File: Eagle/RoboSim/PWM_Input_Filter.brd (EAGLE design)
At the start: 74.6 x 78.7 mm, 72 parts, among them IC1 TLV2772, IC2 TLV2772, IC3 TLV2772

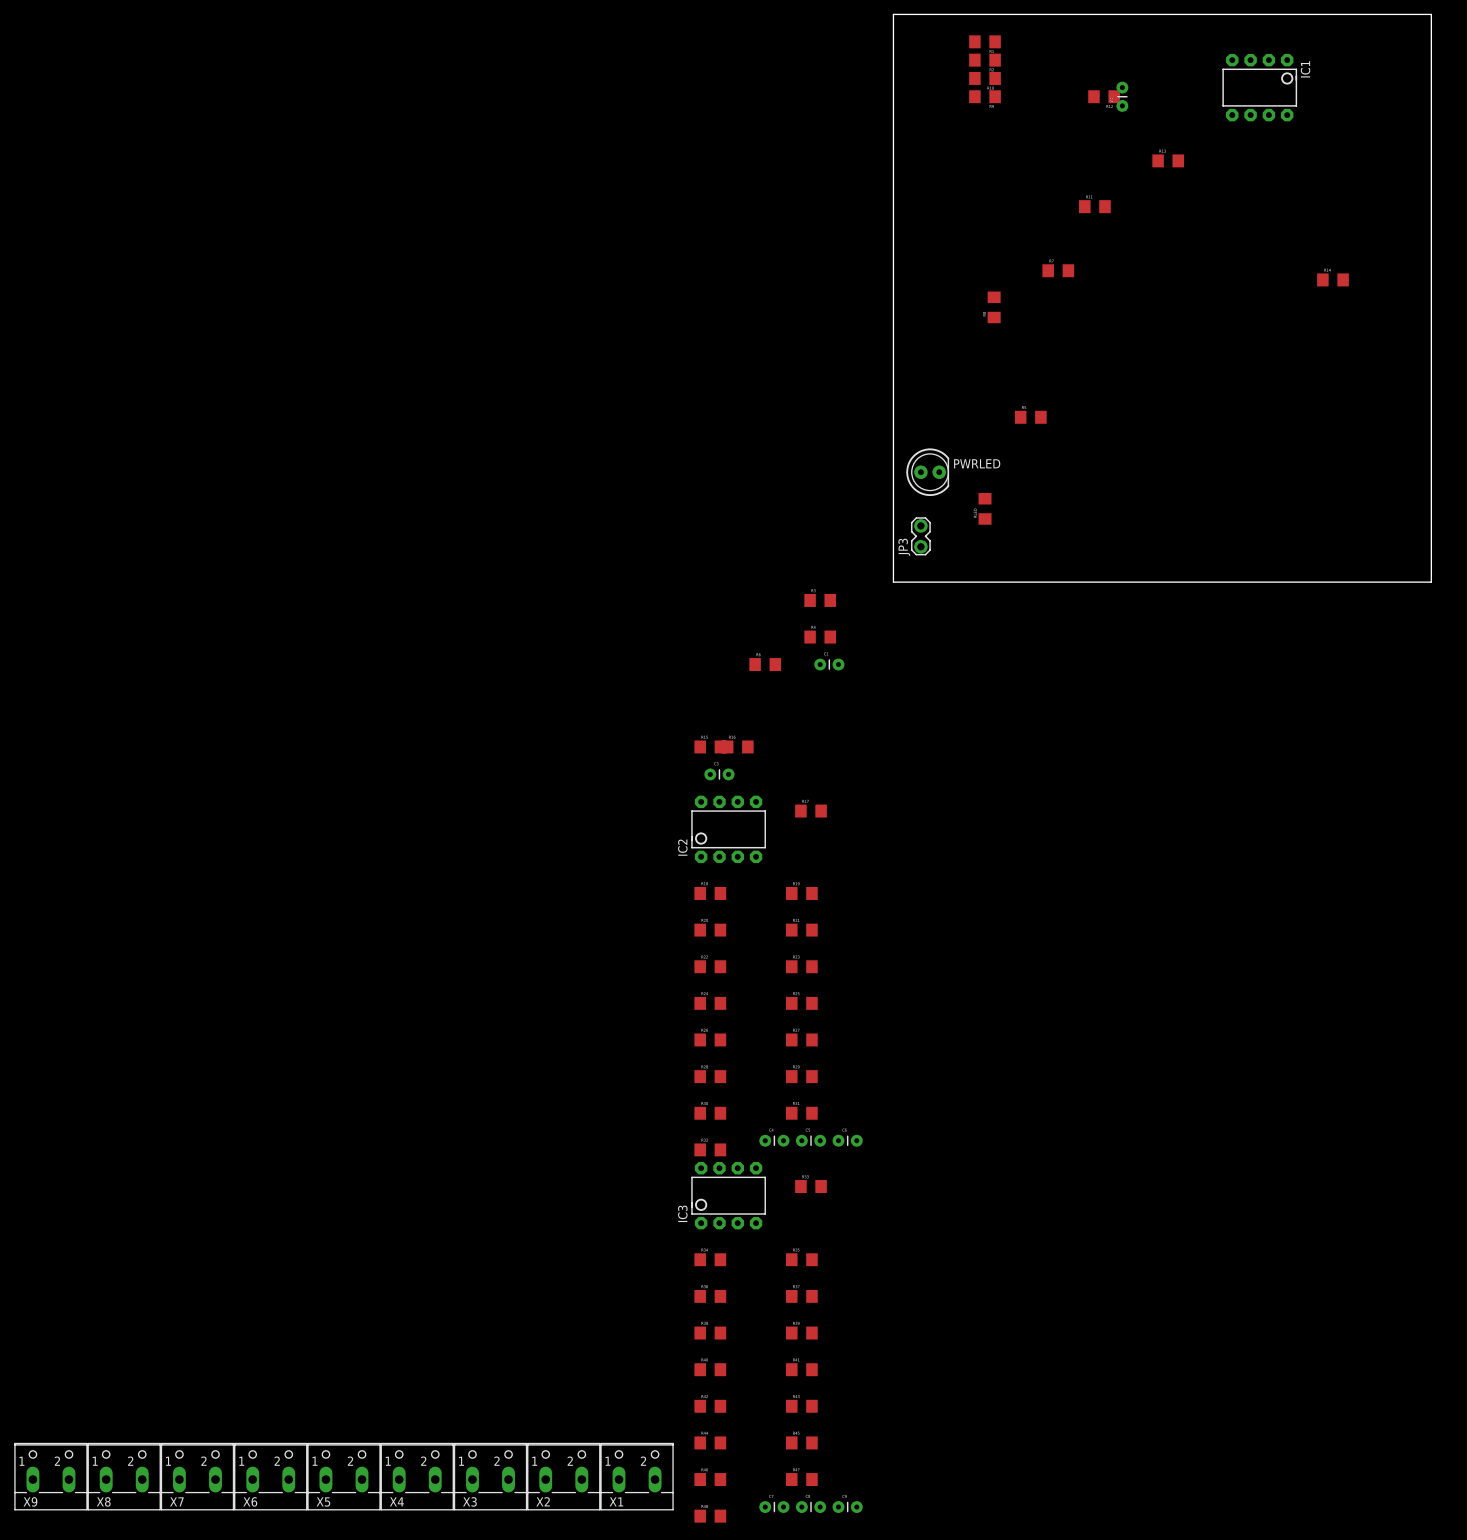
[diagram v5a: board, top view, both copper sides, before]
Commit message: trimmed pwm filter circuit schematic to just show two channels, fixed up schematic
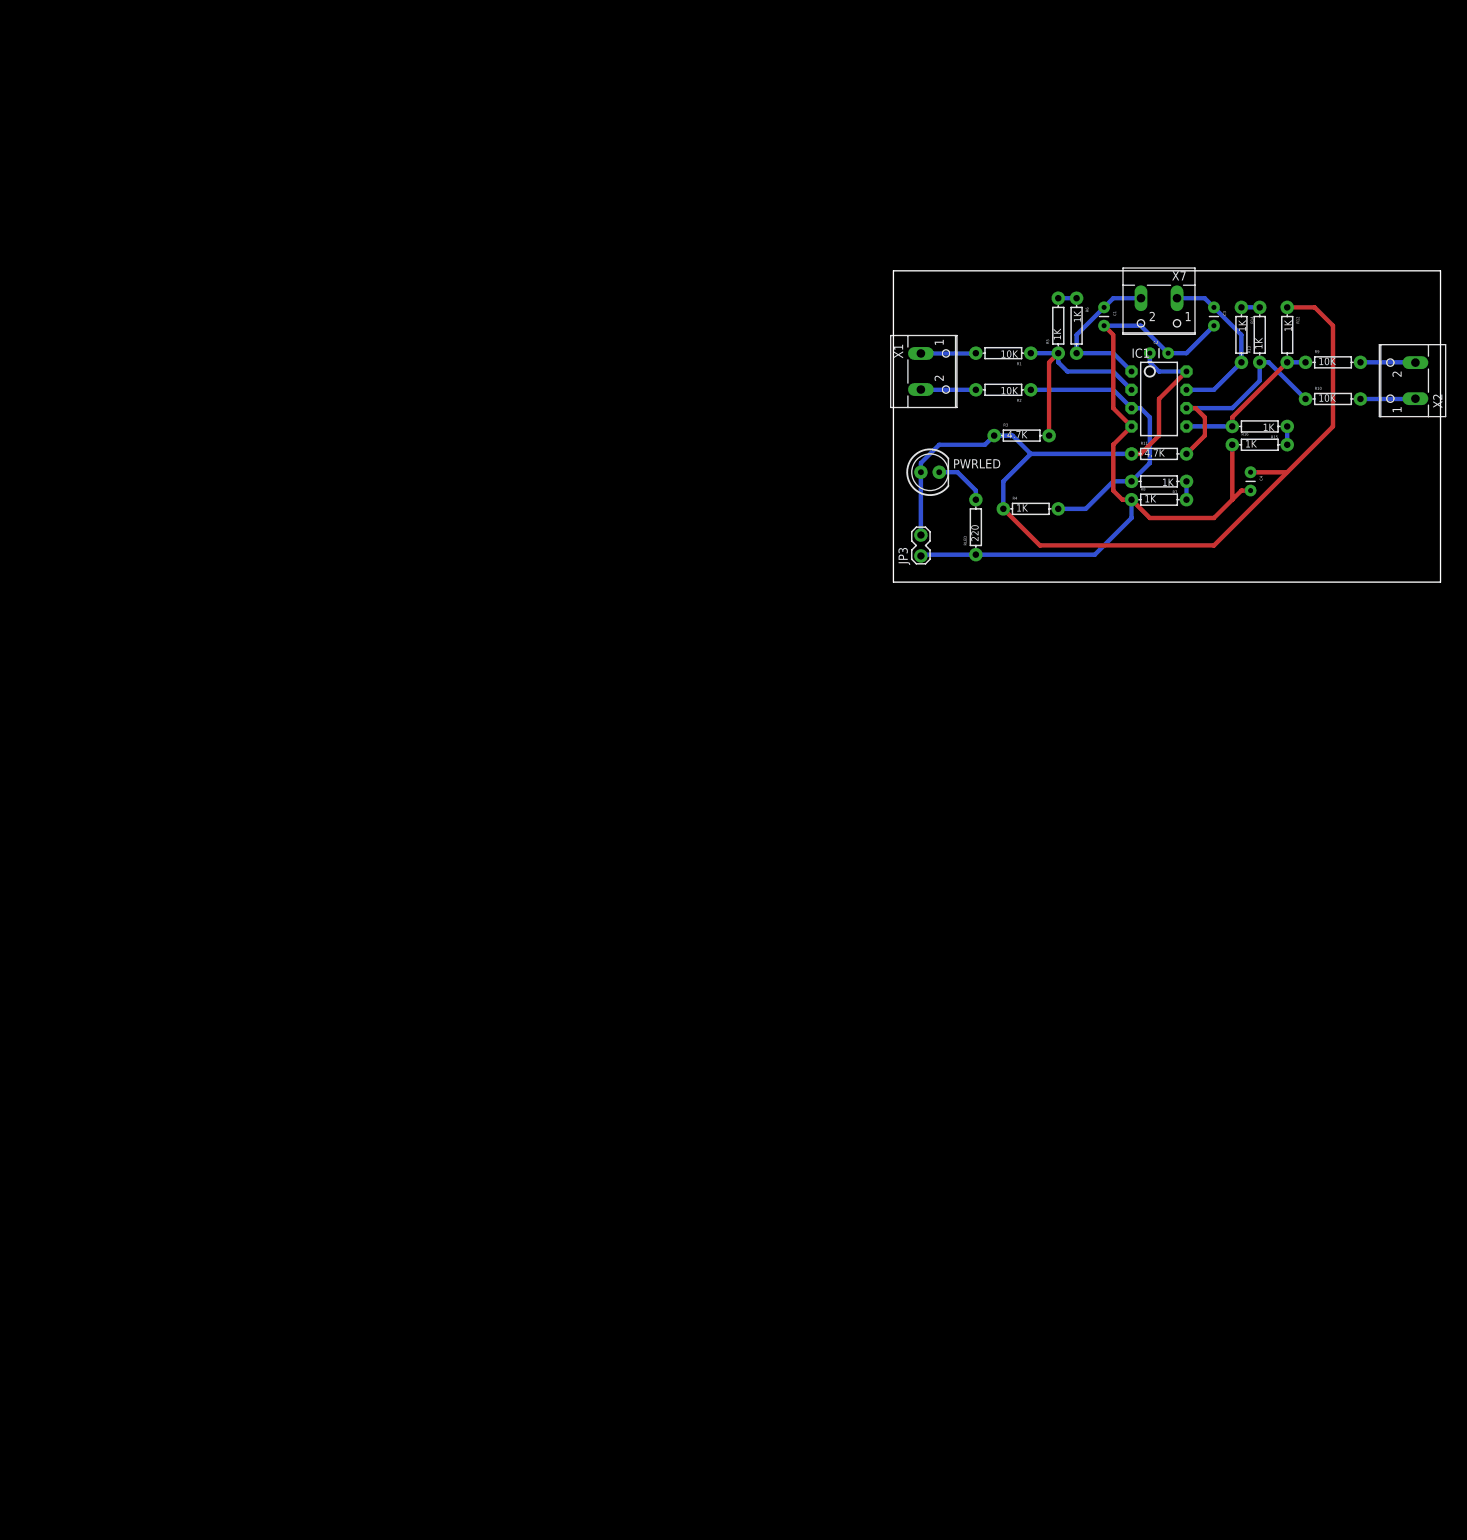
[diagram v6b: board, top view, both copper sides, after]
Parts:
- removed C5, C6, C8, C9: 100uF, SparkFun-Passives:CAP-PTH-SMALL
- removed C7: 3.7uF, SparkFun-Passives:CAP-PTH-SMALL
- removed IC2, IC3: TLV2772, SparkFun-AnalogIC:DIP08
- removed R17, R18, R25, R26, R33, R34, R41, R42: 10K, SparkFun-Passives:1206
- removed R19, R27, R35, R43: 4.7K, SparkFun-Passives:1206
- removed R20, R21, R22, R23, R24, R28, R29, R30, R31, R32, R36, R37, R38, R39, R40, R44, R45, R46, R47, R48: 1K, SparkFun-Passives:1206
- removed X3, X4, X5, X6, X8, X9: (no value), con-wago-500:W237-102
- C4: value 3.7uF -> 100uF
- R1, R10, R11, R12, R13, R14, R15, R16, R2, R3, R4, R5, R6, R7, R8, R9, RLED: device SparkFun-Passives:1206 -> SparkFun-Passives:AXIAL-0.3
- moved X7 209.3 mm to (36.8, 38.1), turned to 180 degrees
- moved X2 191.0 mm to (71.1, 27.9), turned to 90 degrees
- moved X1 157.7 mm to (5.08, 29.2), turned to 270 degrees
- moved C4 114.6 mm to (49.5, 15.2), turned to 270 degrees
- moved C3 95.3 mm to (44.5, 38.1), turned to 270 degrees
- moved R15 88.2 mm to (50.8, 21.6), turned to 180 degrees
- moved R16 83.6 mm to (50.8, 19.1)
- moved R10 65.6 mm to (61.0, 25.4), turned to 0 degrees
- moved R6 63.8 mm to (25.4, 35.6), turned to 270 degrees
- moved C1 63.3 mm to (29.2, 38.1), turned to 270 degrees
- moved R9 60.7 mm to (61.0, 30.5), turned to 0 degrees
- moved R2 45.8 mm to (15.2, 26.7)
- moved IC1 45.4 mm to (36.8, 25.4), turned to 270 degrees
- moved R1 43.3 mm to (15.2, 31.8)
- moved R12 41.7 mm to (54.6, 34.3), turned to 270 degrees
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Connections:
- removed net N$16: R18.2, X3.2
- removed net N$18: C6.1, IC2.7, R30.2, X8.1
- removed net N$2: R17.2, X3.1
- removed net N$20: R25.2, X4.2
- removed net N$21: R9.2, X2.2
- removed net N$22: R26.2, X4.1
- removed net N$24: IC2.2, R18.1, R19.2, R21.1
- removed net N$25: IC2.3, R17.1, R20.2, R23.2
- removed net N$26: R21.2, R22.1
- removed net N$27: R23.1, R24.2
- removed net N$28: IC2.6, R26.1, R27.2, R29.1
- removed net N$29: IC2.5, R25.1, R28.2, R31.2
- removed net N$30: R34.2, X5.1
- removed net N$31: R33.2, X5.2
- removed net N$32: R29.2, R30.1
- removed net N$34: R41.2, X6.2
- removed net N$36: R31.1, R32.2
- removed net N$37: C5.1, IC2.1, R22.2, X8.2
- removed net N$40: C9.1, IC3.7, R46.2, X9.1
- removed net N$41: R42.2, X6.1
- removed net N$43: IC3.2, R34.1, R35.2, R37.1
- removed net N$45: IC3.3, R33.1, R36.2, R39.2
- removed net N$46: R37.2, R38.1
- removed net N$47: R39.1, R40.2
- removed net N$48: IC3.6, R42.1, R43.2, R45.1
- removed net N$49: IC3.5, R41.1, R44.2, R47.2
- removed net N$50: R45.2, R46.1
- removed net N$51: R47.1, R48.2
- removed net N$52: C8.1, IC3.1, R38.2, X9.2
- new net N$3: R9.P$2, X2.2
- net GND: now also R16.P$1, R8.P$1, RLED.P$1; no longer C5.2, C6.2, C7.2, C8.2, C9.2, IC2.4, IC3.4, R16.1, R24.1, R32.1, R40.1, R48.1, R8.1, RLED.1
- net N$1: now also R1.P$2; no longer R1.2
- net N$10: now also R7.P$1, R8.P$2; no longer R7.1, R8.2
- net N$11: now also R10.P$1, R11.P$2, R13.P$1; no longer R10.1, R11.2, R13.1
- net N$12: now also R12.P$2, R15.P$2, R9.P$1; no longer R12.2, R15.2, R9.1
- net N$13: now also R14.P$2; no longer R14.2
- net N$14: now also R10.P$2; no longer R10.2
- net N$15: now also R13.P$2, R14.P$1; no longer R13.2, R14.1
- net N$17: now also R15.P$1, R16.P$2; no longer R15.1, R16.2
- net N$44: now also R6.P$2; no longer R6.2
- net N$5: now also RLED.P$2; no longer RLED.2
- net N$6: now also R1.P$1, R3.P$2, R5.P$1; no longer R1.1, R3.2, R5.1
- net N$7: now also R2.P$1, R4.P$2, R7.P$2; no longer R2.1, R4.2, R7.2
- net N$8: now also R2.P$2; no longer R2.2
- net N$9: now also R5.P$2, R6.P$1; no longer R5.2, R6.1
- net VCC: now also R11.P$1, R12.P$1, R3.P$1, R4.P$1; no longer C7.1, IC2.8, IC3.8, R11.1, R12.1, R19.1, R20.1, R27.1, R28.1, R3.1, R35.1, R36.1, R4.1, R43.1, R44.1
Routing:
- net VCC: track 0.00 -> 154.3 mm
- net GND: track 0.00 -> 107.6 mm
- net N$7: track 0.00 -> 39.8 mm
- net N$11: track 0.00 -> 31.9 mm
- net N$6: track 0.00 -> 28.8 mm
- net N$13: track 0.00 -> 24.0 mm
- net N$44: track 0.00 -> 22.2 mm
- net N$12: track 0.00 -> 20.9 mm
- net N$14: track 0.00 -> 7.64 mm
- net N$3: track 0.00 -> 7.64 mm
- net N$8: track 0.00 -> 7.64 mm
- net N$1: track 0.00 -> 7.64 mm
- net N$5: track 0.00 -> 7.40 mm
- net N$10: track 0.00 -> 2.54 mm
- net N$9: track 0.00 -> 2.54 mm
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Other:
- board size 74.6 x 78.7 mm -> 75.9 x 43.2 mm

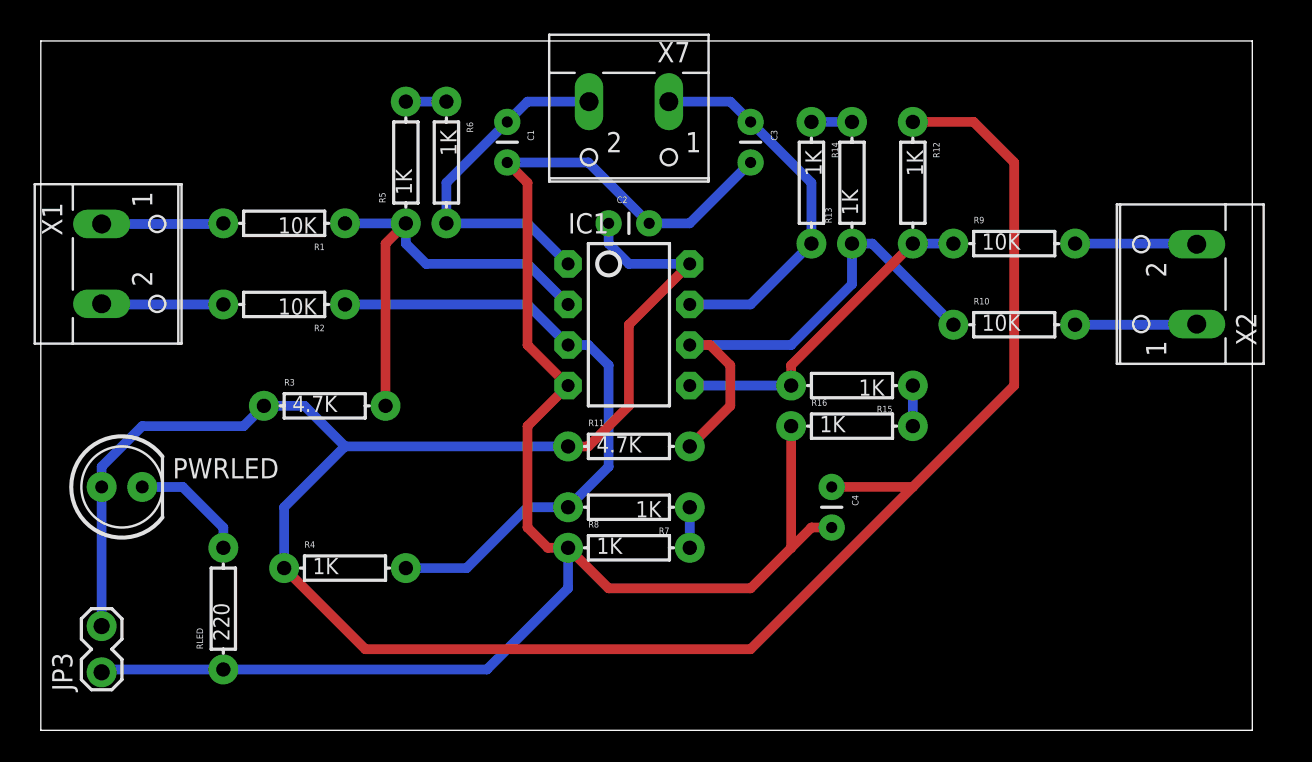
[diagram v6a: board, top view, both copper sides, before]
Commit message: added extra text to schematic
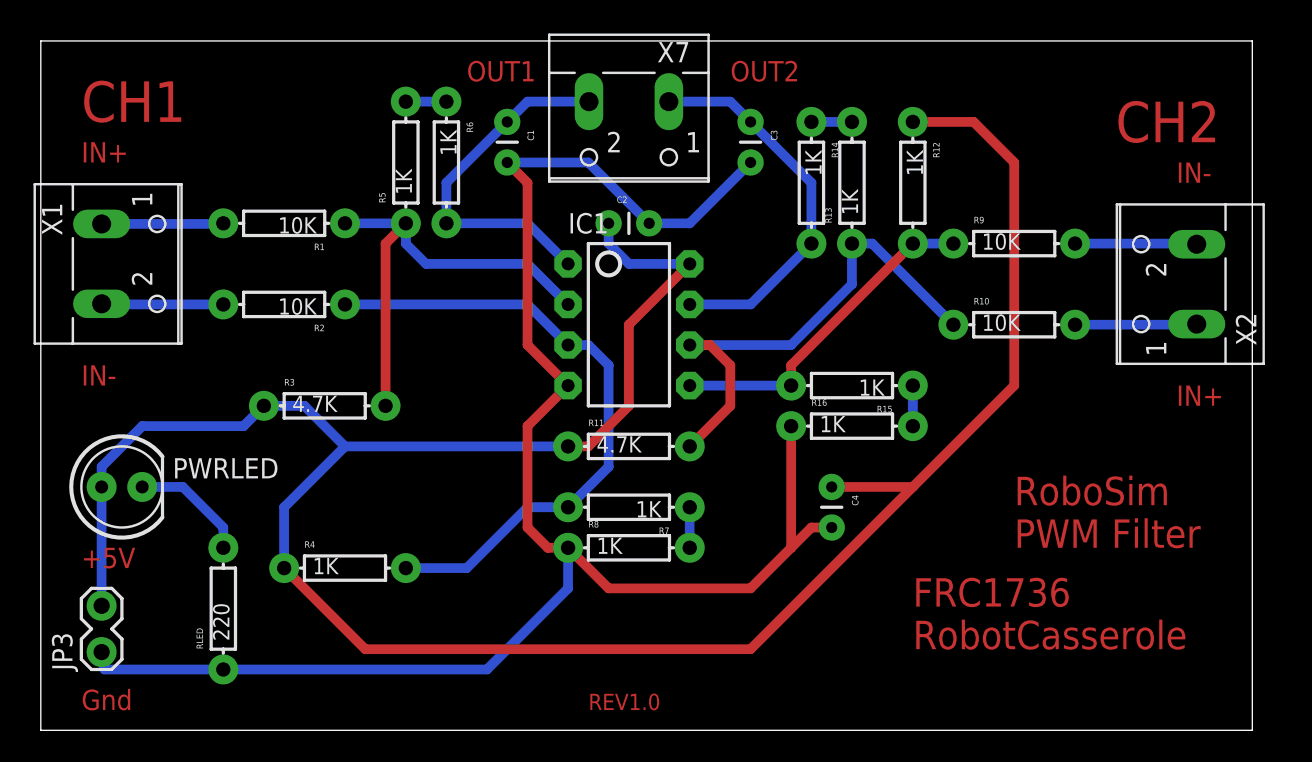
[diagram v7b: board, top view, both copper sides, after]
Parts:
- JP3: value M02LOCK -> PWR_IN
- moved JP3 1.27 mm to (3.81, 5.08)
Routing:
- net VCC: track 154.3 -> 153.1 mm
- net GND: track 107.6 -> 108.5 mm
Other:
- board text added: "+5V"
- board text added: "CH1"
- board text added: "CH2"
- board text added: "FRC1736 RobotCasserole"
- board text added: "Gnd"
- board text added: "IN+"
- board text added: "IN-"
- board text added: "OUT1"
- board text added: "OUT2"
- board text added: "REV1.0"
- board text added: "RoboSim PWM Filter"
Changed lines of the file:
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@@
 <wire x1="75.87" y1="43.17" x2="0" y2="43.17" width="0" layer="20"/>
 <wire x1="0" y1="43.17" x2="0" y2="0" width="0" layer="20"/>
+<text x="54.61" y="5.08" size="1.778" layer="1">FRC1736
+RobotCasserole</text>
+<text x="60.96" y="11.43" size="1.778" layer="1">RoboSim
+PWM Filter</text>
+<text x="2.54" y="38.1" size="2.54" layer="1">CH1</text>
+<text x="67.31" y="36.83" size="2.54" layer="1">CH2</text>
+<text x="2.54" y="35.56" size="1.27" layer="1">IN+</text>
+<text x="71.12" y="20.32" size="1.27" layer="1">IN+</text>
+<text x="2.54" y="21.59" size="1.27" layer="1">IN-</text>
+<text x="71.12" y="34.29" size="1.27" layer="1">IN-</text>
+<text x="26.67" y="40.64" size="1.27" layer="1">OUT1</text>
+<text x="43.18" y="40.64" size="1.27" layer="1">OUT2</text>
+<text x="2.54" y="10.16" size="1.27" layer="1">+5V</text>
+<text x="2.54" y="1.27" size="1.27" layer="1">Gnd</text>
+<text x="34.29" y="1.27" size="1.016" layer="1">REV1.0</text>
 </plain>
 <attributes>
@@
 <attribute name="PROD_ID" value="IC-09172" x="31.75" y="6.35" size="1.778" layer="27" rot="R270" display="off"/>
 </element>
-<element name="JP3" library="SparkFun-Connectors" package="1X02_LOCK" value="M02LOCK" x="3.81" y="3.81" rot="R90"/>
+<element name="JP3" library="SparkFun-Connectors" package="1X02_LOCK" value="PWR_IN" x="3.81" y="5.08" rot="R90"/>
 <element name="C2" library="SparkFun-Passives" package="CAP-PTH-SMALL" value="3.7uF" x="35.56" y="31.75"/>
 <element name="PWRLED" library="SparkFun-LED" package="LED5MM" value="Red" x="5.08" y="15.24"/>
@@
 <contactref element="R11" pad="P$1"/>
 <contactref element="R12" pad="P$1"/>
-<wire x1="3.81" y1="6.5278" x2="3.81" y2="15.24" width="0.6096" layer="16"/>
+<wire x1="3.81" y1="7.7978" x2="3.81" y2="15.24" width="0.6096" layer="16"/>
 <wire x1="3.81" y1="15.24" x2="3.81" y2="16.51" width="0.6096" layer="16"/>
 <wire x1="35.56" y1="31.75" x2="35.56" y2="30.48" width="0.6096" layer="16"/>
@@
 <contactref element="C3" pad="2"/>
 <wire x1="11.43" y1="3.81" x2="3.9878" y2="3.81" width="0.6096" layer="16"/>
-<wire x1="3.9878" y1="3.81" x2="3.81" y2="3.6322" width="0.6096" layer="16"/>
+<wire x1="3.9878" y1="3.81" x2="3.81" y2="4.9022" width="0.6096" layer="16"/>
 <wire x1="11.43" y1="3.81" x2="27.94" y2="3.81" width="0.6096" layer="16"/>
 <wire x1="27.94" y1="3.81" x2="33.02" y2="8.89" width="0.6096" layer="16"/>
@@
 </board>
 </drawing>
+<compatibility>
+<note version="6.3" minversion="6.2.2" severity="warning">
+Since Version 6.2.2 text objects can contain more than one line,
+which will not be processed correctly with this version.
+</note>
+</compatibility>
 </eagle>
